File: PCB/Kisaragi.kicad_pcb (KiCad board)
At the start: 2 copper layers, 299.7 x 145.8 mm, 112 parts, among them SW1 SW_PUSH, SW10 SW_PUSH, SW11 SW_PUSH, SW12 SW_PUSH, SW13 SW_PUSH, SW14 SW_PUSH, SW15 SW_PUSH, SW16 SW_PUSH, SW17 SW_PUSH, SW18 SW_PUSH, SW19 SW_PUSH, SW2 SW_PUSH, SW20 SW_PUSH, SW21 SW_PUSH, SW22 SW_PUSH, SW23 SW_PUSH, SW24 SW_PUSH, SW25 SW_PUSH, SW26 SW_PUSH, SW27 SW_PUSH, SW28 SW_PUSH, SW29 SW_PUSH, SW3 SW_PUSH, SW30 SW_PUSH, SW31 SW_PUSH, SW32 SW_PUSH, SW33 SW_PUSH, SW34 SW_PUSH, SW35 SW_PUSH, SW36 SW_PUSH, SW37 SW_PUSH, SW38 SW_PUSH, SW39 SW_PUSH, SW4 SW_PUSH, SW40 SW_PUSH, SW41 SW_PUSH, SW42 SW_PUSH, SW43 SW_PUSH, SW44 SW_PUSH, SW45 SW_PUSH, SW46 SW_PUSH, SW47 SW_PUSH, SW48 SW_PUSH, SW49 SW_PUSH, SW5 SW_PUSH, SW50 SW_PUSH, SW51 SW_PUSH, SW52 SW_PUSH, SW53 reset, SW6 SW_PUSH, SW7 SW_PUSH, SW8 SW_PUSH, SW9 SW_PUSH, U1 ProMicro

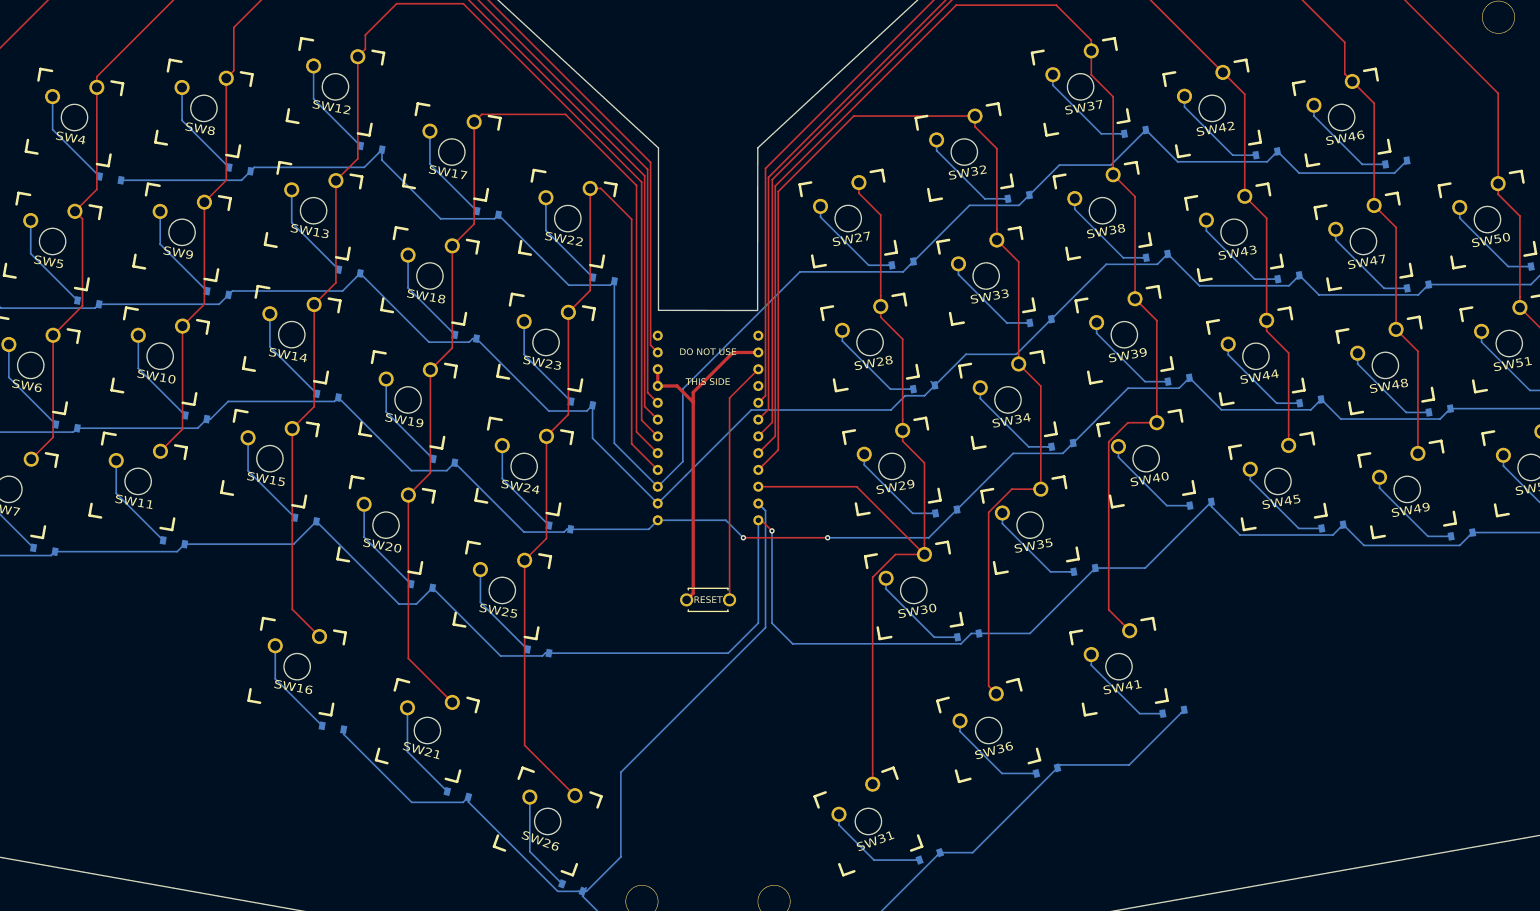
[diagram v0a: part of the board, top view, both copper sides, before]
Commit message: added logos
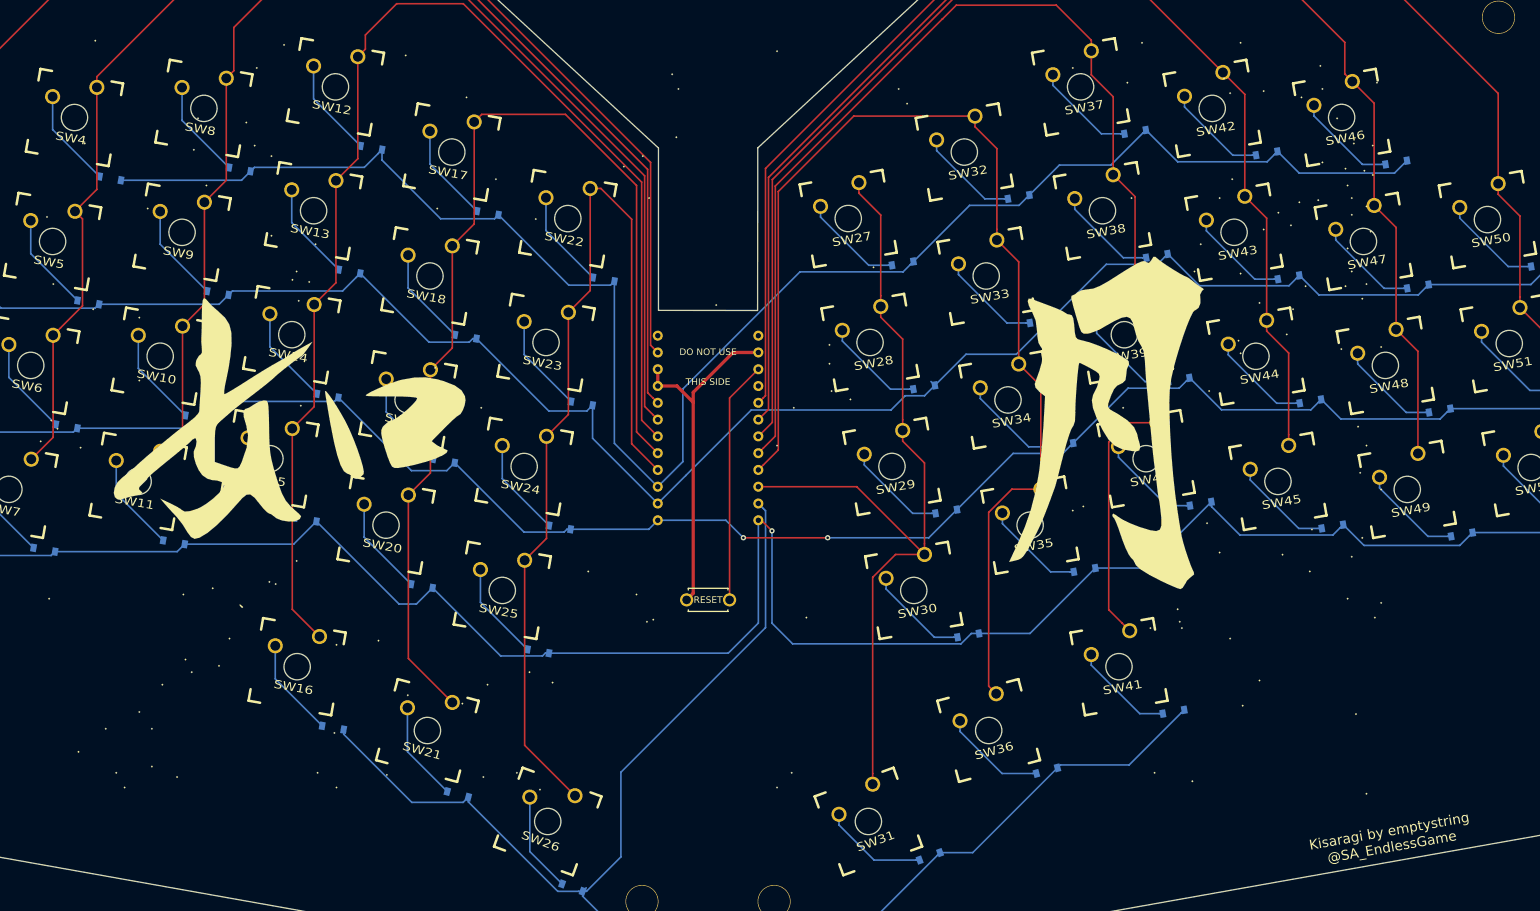
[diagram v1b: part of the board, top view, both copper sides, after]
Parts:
- added G***: LOGO, Kisaragi:Kisaragi, F.Cu at (215.7, 158.8)
- added G***: LOGO, Kisaragi:emptystringLogo, B.Cu at (208.5, 215.8)
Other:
- board text added: "Kisaragi by emptystring @SA_EndlessGame"

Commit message: added LED strip support
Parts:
- removed Ref** (x6): Val**, kbd:HOLE
- added J1: Conn_01x03, kbd:LEDStrip, B.Cu at (276.4, 220.8)
- added J2: Conn_01x03, kbd:LEDStrip, B.Cu at (155.6, 220.6)
- moved G*** 11.9 mm to (200.4, 207.0)
- moved G*** 5.91 mm to (215.7, 164.7)
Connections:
- U1 pad 1: Net-(U1-Pad1) -> LED
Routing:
- net LED: track 0.00 -> 307.4 mm, vias 0 -> 2
- net VCC: track 0.00 -> 291.1 mm, vias 0 -> 1
- net GND: track 53.1 -> 322.9 mm, vias 0 -> 1
- net row4: track 226.0 -> 222.0 mm
- removed copper zone on B.Cu, net GND
